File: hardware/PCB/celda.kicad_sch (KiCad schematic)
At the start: 22 parts, among them Q11_1 MMBT2222A, Q11_2 MMBT2907A, Q11_3 MMBT2222A

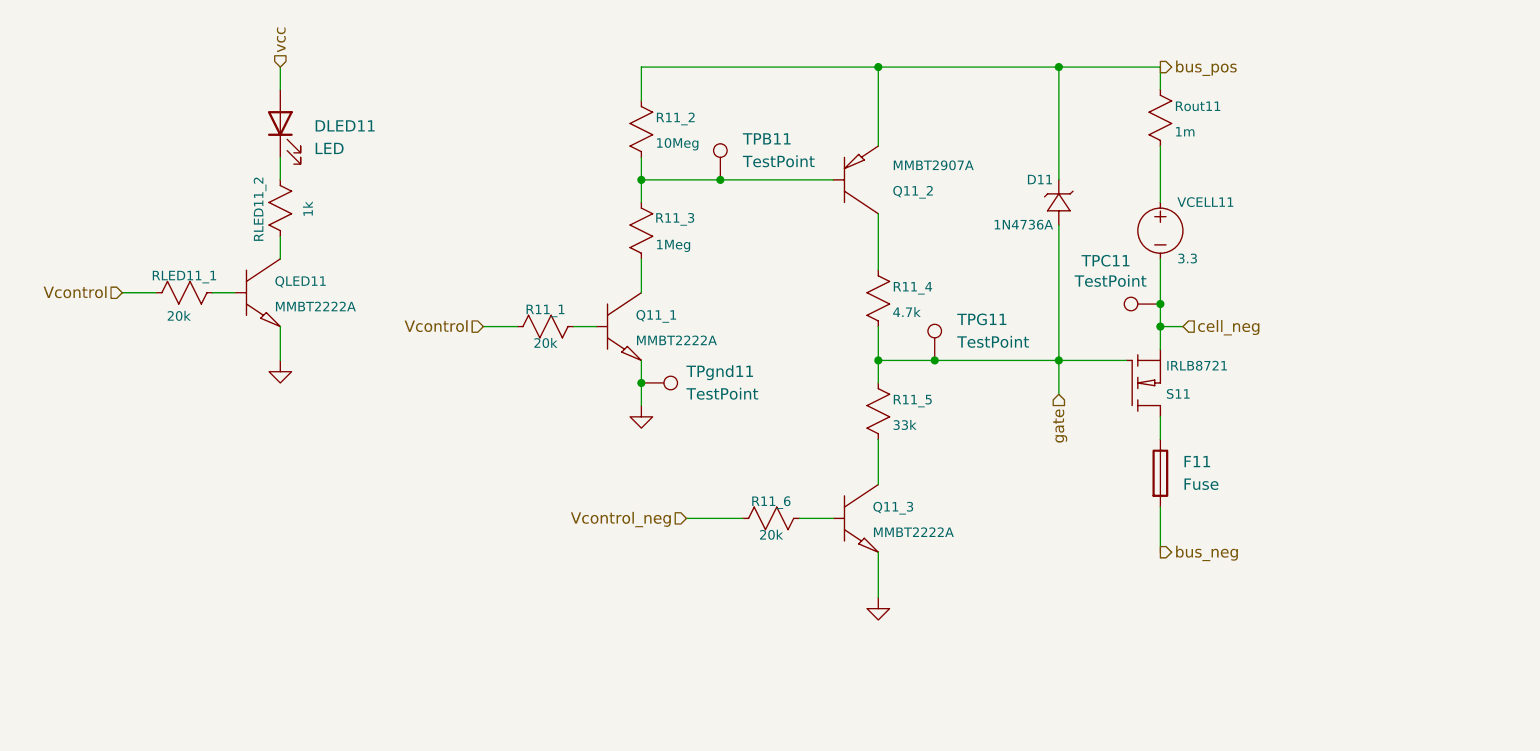
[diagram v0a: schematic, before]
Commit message: agranda los pads de las vias a 1.7mm
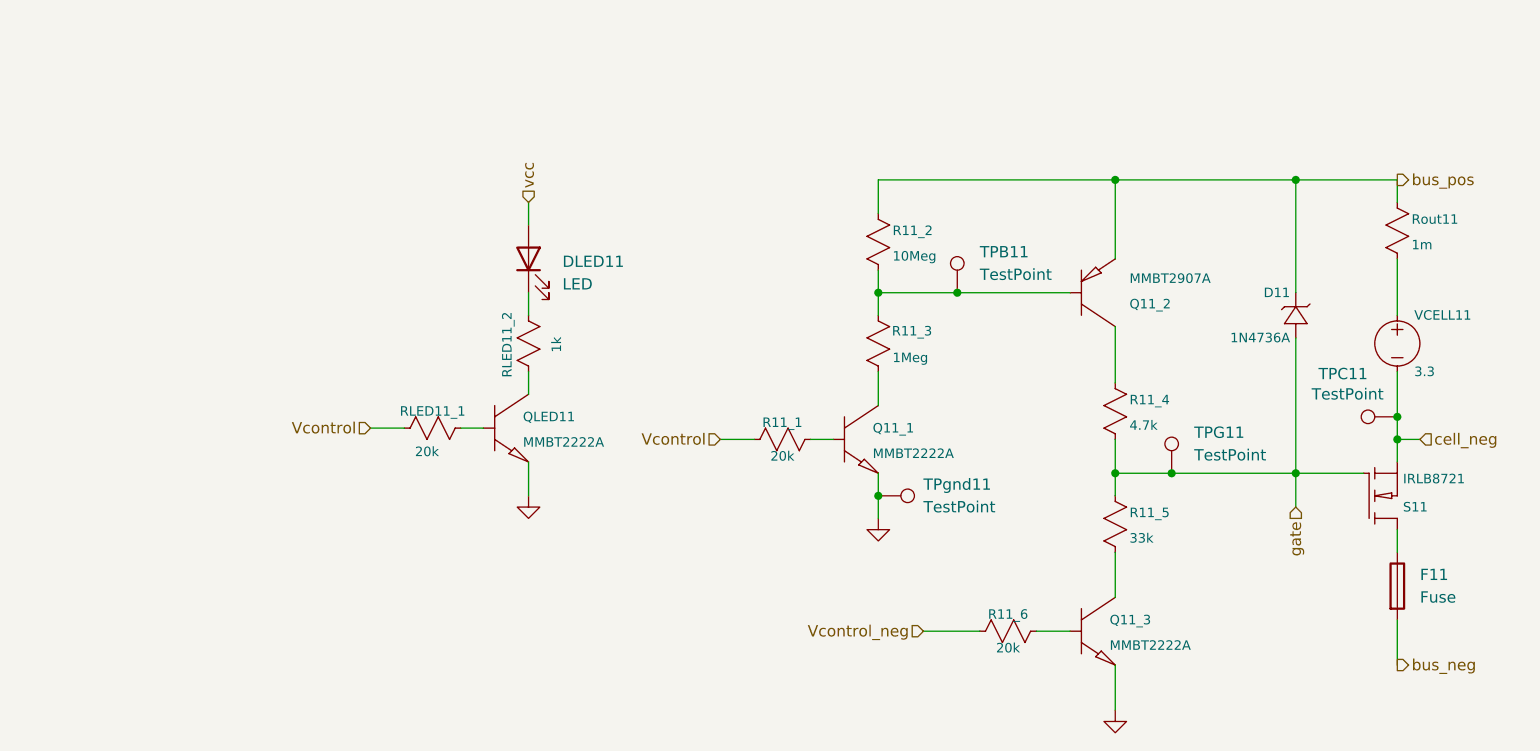
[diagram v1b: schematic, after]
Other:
- moved on the sheet: D11, DLED11, F11, Q11_1, Q11_2, Q11_3, QLED11, R11_1, R11_2, R11_3, R11_4, R11_5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
